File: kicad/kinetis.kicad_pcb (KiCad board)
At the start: 2 copper layers, 88.9 x 88.9 mm, 82 parts, among them J1 FTDI_Connector, J2 CONN_01X16, J3 USB_Micro_B, J4 CONN_01X16, J5 JLink_SWD_20pin, J6 CONN_01X16, J7 CONN_01X16, M1 #4-40 Mounting Hole, M2 #4-40 Mounting Hole, M3 #4-40 Mounting Hole, M4 #4-40 Mounting Hole, SW1 DPDT, SW2 SPST, SW3 SPST, SW4 SPST, SW5 SPST, SW6 SPST, U1 LM1117-ADJ, U2 MKL16Z64VLH4, Y1 12.000 MHz

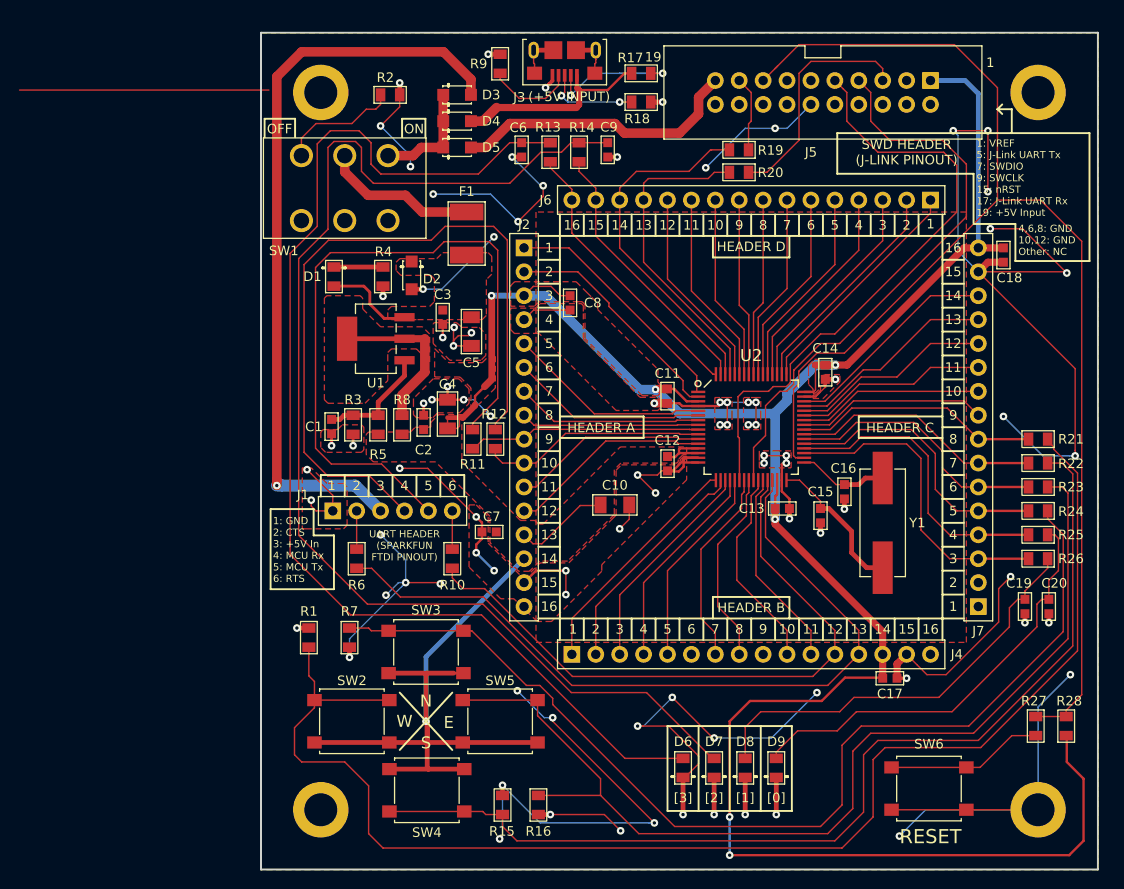
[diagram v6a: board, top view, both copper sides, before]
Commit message: Added a couple more stitch vias
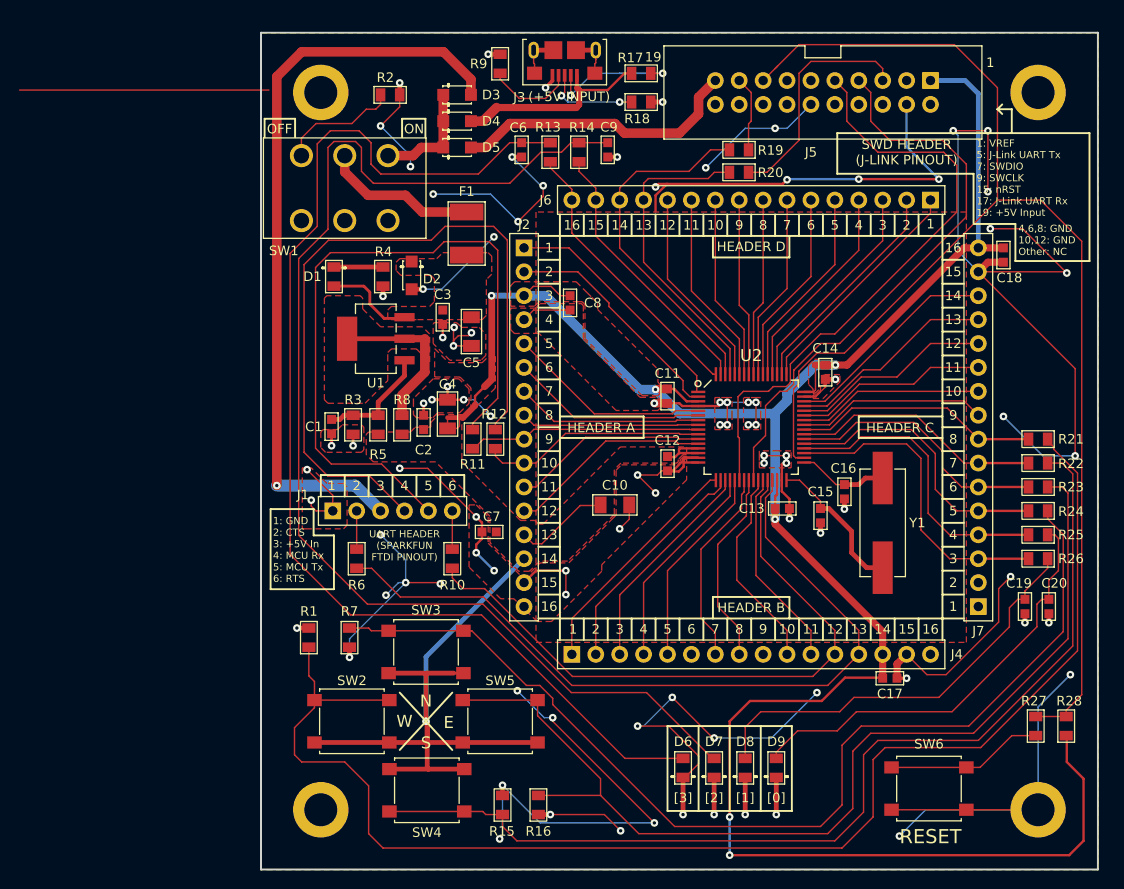
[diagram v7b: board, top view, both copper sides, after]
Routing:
- net GND: track 473.9 -> 517.1 mm, vias 89 -> 93

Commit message: Updated parts to use whiteliseted hole sizes
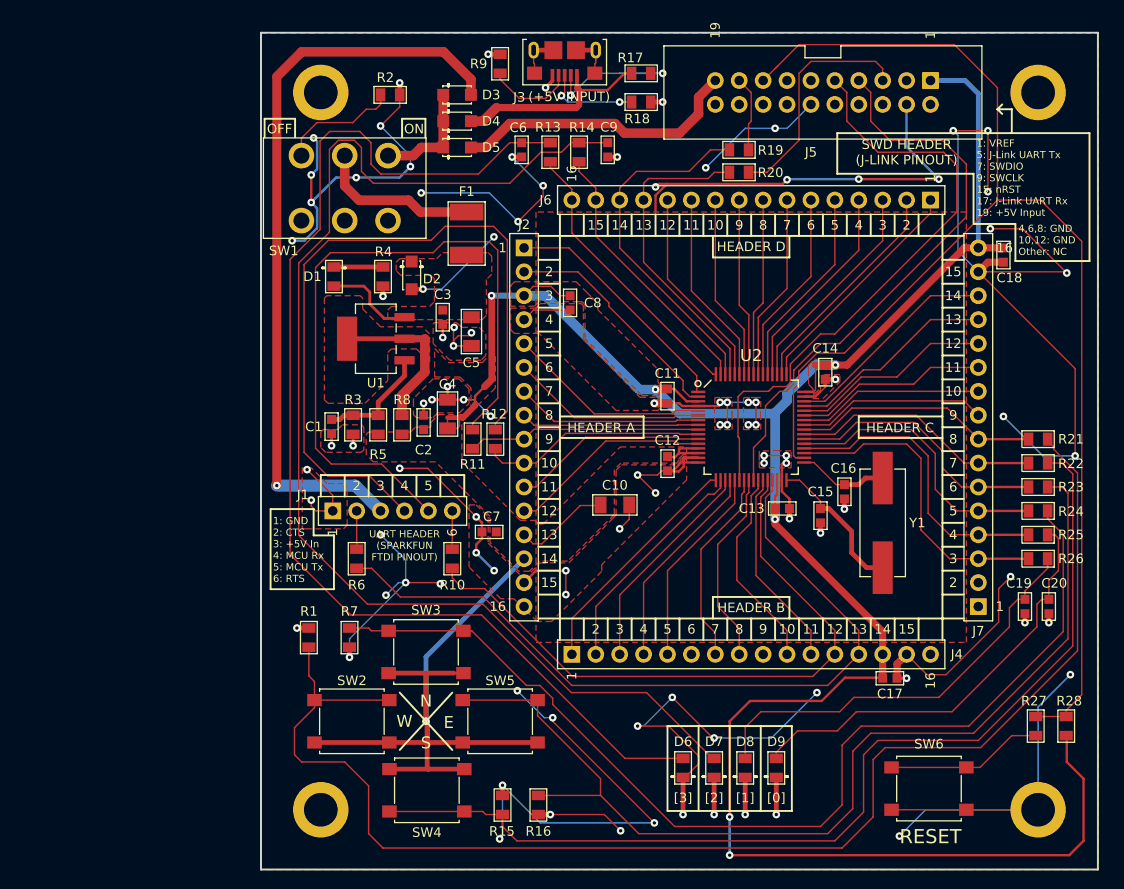
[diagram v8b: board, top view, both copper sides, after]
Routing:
- net (no net): track 26.5 -> 0.00 mm
- net GND: track 517.1 -> 541.1 mm, vias 93 -> 98
- net Net-(F1-Pad2): track 16.4 -> 17.3 mm
